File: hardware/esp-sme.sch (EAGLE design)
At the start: 37 parts, among them J2 BME280, J3 UART, Q1 MOSFET-NCH-AO3404A, Q2 MOSFET-NCH-AO3404A, Q3 NPN, Q4 NPN, Q5 NPN, U2 MIC5504

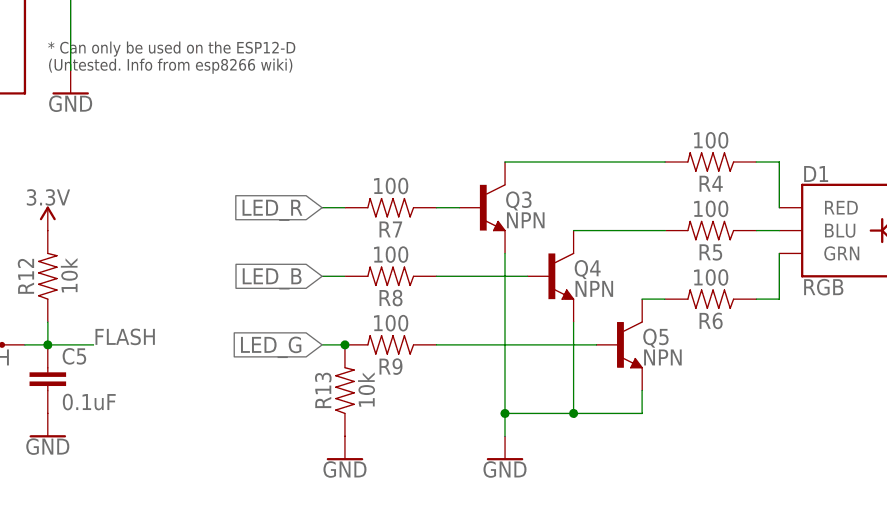
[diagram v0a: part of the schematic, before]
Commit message: Replaced transistor for n-channel mosfet
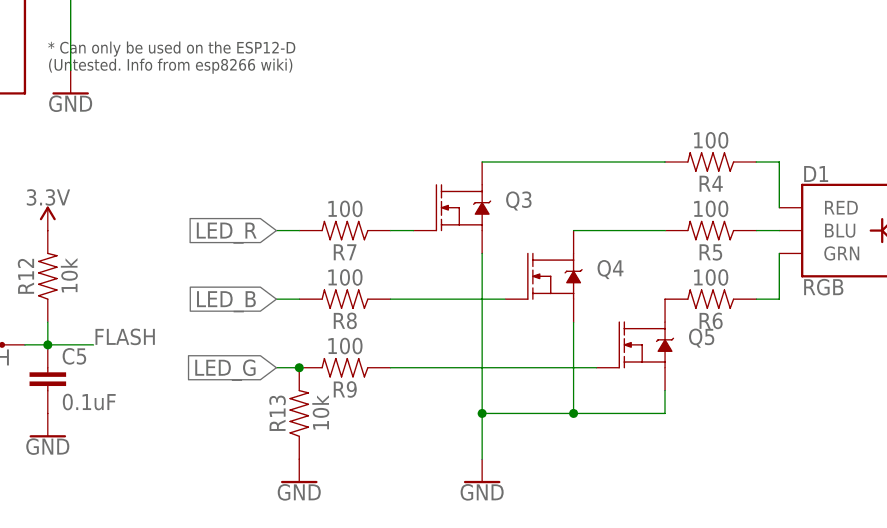
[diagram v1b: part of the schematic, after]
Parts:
- Q3, Q4, Q5: value NPN -> MOSFET-NCH-AO3404A; device SparkFun-DiscreteSemi:TRANS_NPN-MMBT2222AL -> SparkFun-DiscreteSemi:MOSFET-NCH-AO3404A
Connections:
- net GND: now also Q3.S, Q4.S, Q5.S; no longer Q3.E, Q4.E, Q5.E
- net N$4: now also Q5.D; no longer Q5.C
- net N$5: now also Q4.D; no longer Q4.C
- net N$6: now also Q3.D; no longer Q3.C
- net N$7: now also Q5.G; no longer Q5.B
- net N$8: now also Q4.G; no longer Q4.B
- net N$9: now also Q3.G; no longer Q3.B
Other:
- moved on the sheet: R13, R7, R8, R9
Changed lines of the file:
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@@
 <part name="R6" library="SparkFun-Resistors" library_urn="urn:adsk.eagle:library:532" deviceset="100OHM" device="-0603-1/10W-1%" package3d_urn="urn:adsk.eagle:package:39650/1" value="100"/>
 <part name="SUPPLY8" library="SparkFun-PowerSymbols" library_urn="urn:adsk.eagle:library:530" deviceset="3.3V" device=""/>
-<part name="Q3" library="SparkFun-DiscreteSemi" library_urn="urn:adsk.eagle:library:514" deviceset="TRANS_NPN" device="-MMBT2222AL" package3d_urn="urn:adsk.eagle:package:38446/1" value="NPN"/>
-<part name="Q4" library="SparkFun-DiscreteSemi" library_urn="urn:adsk.eagle:library:514" deviceset="TRANS_NPN" device="-MMBT2222AL" package3d_urn="urn:adsk.eagle:package:38446/1" value="NPN"/>
-<part name="Q5" library="SparkFun-DiscreteSemi" library_urn="urn:adsk.eagle:library:514" deviceset="TRANS_NPN" device="-MMBT2222AL" package3d_urn="urn:adsk.eagle:package:38446/1" value="NPN"/>
 <part name="R7" library="SparkFun-Resistors" library_urn="urn:adsk.eagle:library:532" deviceset="100OHM" device="-0603-1/10W-1%" package3d_urn="urn:adsk.eagle:package:39650/1" value="100"/>
 <part name="R8" library="SparkFun-Resistors" library_urn="urn:adsk.eagle:library:532" deviceset="100OHM" device="-0603-1/10W-1%" package3d_urn="urn:adsk.eagle:package:39650/1" value="100"/>
@@
 <part name="R14" library="SparkFun-Resistors" library_urn="urn:adsk.eagle:library:532" deviceset="10KOHM" device="-0603-1/10W-1%" package3d_urn="urn:adsk.eagle:package:39650/1" value="10k"/>
 <part name="R15" library="SparkFun-Resistors" library_urn="urn:adsk.eagle:library:532" deviceset="10KOHM" device="-0603-1/10W-1%" package3d_urn="urn:adsk.eagle:package:39650/1" value="10k"/>
+<part name="Q3" library="SparkFun-DiscreteSemi" library_urn="urn:adsk.eagle:library:514" deviceset="MOSFET-NCH" device="-AO3404A" package3d_urn="urn:adsk.eagle:package:38446/1" value=""/>
+<part name="Q4" library="SparkFun-DiscreteSemi" library_urn="urn:adsk.eagle:library:514" deviceset="MOSFET-NCH" device="-AO3404A" package3d_urn="urn:adsk.eagle:package:38446/1" value=""/>
+<part name="Q5" library="SparkFun-DiscreteSemi" library_urn="urn:adsk.eagle:library:514" deviceset="MOSFET-NCH" device="-AO3404A" package3d_urn="urn:adsk.eagle:package:38446/1" value=""/>
 </parts>
 <sheets>
@@
 <instance part="R6" gate="G$1" x="101.6" y="-10.16" rot="R180"/>
 <instance part="SUPPLY8" gate="G$1" x="132.08" y="5.08"/>
-<instance part="Q3" gate="G$1" x="76.2" y="0"/>
-<instance part="Q4" gate="G$1" x="83.82" y="-7.62"/>
-<instance part="Q5" gate="G$1" x="91.44" y="-15.24"/>
-<instance part="R7" gate="G$1" x="66.04" y="0" rot="R180"/>
-<instance part="R8" gate="G$1" x="66.04" y="-7.62" rot="R180"/>
-<instance part="R9" gate="G$1" x="66.04" y="-15.24" rot="R180"/>
-<instance part="GND9" gate="1" x="78.74" y="-27.94"/>
+<instance part="R7" gate="G$1" x="60.96" y="-2.54" rot="R180"/>
+<instance part="R8" gate="G$1" x="60.96" y="-10.16" rot="R180"/>
+<instance part="R9" gate="G$1" x="60.96" y="-17.78" rot="R180"/>
+<instance part="GND9" gate="1" x="76.2" y="-30.48"/>
 <instance part="J2" gate="G$1" x="86.36" y="38.1" rot="R180"/>
 <instance part="SUPPLY9" gate="G$1" x="78.74" y="50.8"/>
@@
 <instance part="C5" gate="G$1" x="27.94" y="-20.32"/>
 <instance part="GND15" gate="1" x="27.94" y="-25.4"/>
-<instance part="R13" gate="G$1" x="60.96" y="-20.32" rot="R90"/>
-<instance part="GND16" gate="1" x="60.96" y="-27.94"/>
+<instance part="R13" gate="G$1" x="55.88" y="-22.86" rot="R90"/>
+<instance part="GND16" gate="1" x="55.88" y="-30.48"/>
 <instance part="R14" gate="G$1" x="73.66" y="45.72" rot="R90"/>
 <instance part="R15" gate="G$1" x="66.04" y="45.72" rot="R90"/>
+<instance part="Q3" gate="NMOS" x="73.66" y="0"/>
+<instance part="Q4" gate="NMOS" x="83.82" y="-7.62"/>
+<instance part="Q5" gate="NMOS" x="93.98" y="-15.24"/>
 </instances>
 <busses>
@@
 </segment>
 <segment>
-<pinref part="Q3" gate="G$1" pin="E"/>
-<wire x1="78.74" y1="-5.08" x2="78.74" y2="-22.86" width="0.1524" layer="91"/>
+<wire x1="76.2" y1="-5.08" x2="76.2" y2="-22.86" width="0.1524" layer="91"/>
 <pinref part="GND9" gate="1" pin="GND"/>
-<pinref part="Q4" gate="G$1" pin="E"/>
-<wire x1="78.74" y1="-22.86" x2="78.74" y2="-25.4" width="0.1524" layer="91"/>
+<wire x1="76.2" y1="-22.86" x2="76.2" y2="-27.94" width="0.1524" layer="91"/>
 <wire x1="86.36" y1="-12.7" x2="86.36" y2="-22.86" width="0.1524" layer="91"/>
-<pinref part="Q5" gate="G$1" pin="E"/>
-<wire x1="93.98" y1="-20.32" x2="93.98" y2="-22.86" width="0.1524" layer="91"/>
-<wire x1="93.98" y1="-22.86" x2="86.36" y2="-22.86" width="0.1524" layer="91"/>
-<wire x1="86.36" y1="-22.86" x2="78.74" y2="-22.86" width="0.1524" layer="91"/>
+<wire x1="96.52" y1="-20.32" x2="96.52" y2="-22.86" width="0.1524" layer="91"/>
+<wire x1="96.52" y1="-22.86" x2="86.36" y2="-22.86" width="0.1524" layer="91"/>
+<wire x1="86.36" y1="-22.86" x2="76.2" y2="-22.86" width="0.1524" layer="91"/>
 <junction x="86.36" y="-22.86"/>
-<junction x="78.74" y="-22.86"/>
+<junction x="76.2" y="-22.86"/>
+<pinref part="Q3" gate="NMOS" pin="S"/>
+<pinref part="Q4" gate="NMOS" pin="S"/>
+<pinref part="Q5" gate="NMOS" pin="S"/>
 </segment>
 <segment>
@@
 <segment>
 <pinref part="R7" gate="G$1" pin="2"/>
-<wire x1="60.96" y1="0" x2="58.42" y2="0" width="0.1524" layer="91"/>
-<label x="58.42" y="0" size="1.778" layer="95" rot="R180" xref="yes"/>
+<wire x1="55.88" y1="-2.54" x2="53.34" y2="-2.54" width="0.1524" layer="91"/>
+<label x="53.34" y="-2.54" size="1.778" layer="95" rot="R180" xref="yes"/>
 </segment>
 </net>
@@
 <segment>
 <pinref part="R8" gate="G$1" pin="2"/>
-<wire x1="60.96" y1="-7.62" x2="58.42" y2="-7.62" width="0.1524" layer="91"/>
-<label x="58.42" y="-7.62" size="1.778" layer="95" rot="R180" xref="yes"/>
+<wire x1="55.88" y1="-10.16" x2="53.34" y2="-10.16" width="0.1524" layer="91"/>
+<label x="53.34" y="-10.16" size="1.778" layer="95" rot="R180" xref="yes"/>
 </segment>
 </net>
@@
 <segment>
 <pinref part="R9" gate="G$1" pin="2"/>
-<wire x1="60.96" y1="-15.24" x2="58.42" y2="-15.24" width="0.1524" layer="91"/>
-<label x="58.42" y="-15.24" size="1.778" layer="95" rot="R180" xref="yes"/>
+<wire x1="55.88" y1="-17.78" x2="53.34" y2="-17.78" width="0.1524" layer="91"/>
+<label x="53.34" y="-17.78" size="1.778" layer="95" rot="R180" xref="yes"/>
 <pinref part="R13" gate="G$1" pin="2"/>
-<junction x="60.96" y="-15.24"/>
-</segment>
-</net>
-<net name="N$4" class="0">
-<segment>
-<pinref part="R6" gate="G$1" pin="2"/>
-<pinref part="Q5" gate="G$1" pin="C"/>
-<wire x1="96.52" y1="-10.16" x2="93.98" y2="-10.16" width="0.1524" layer="91"/>
+<junction x="55.88" y="-17.78"/>
 </segment>
 </net>
@@
 <segment>
 <pinref part="R5" gate="G$1" pin="2"/>
-<pinref part="Q4" gate="G$1" pin="C"/>
 <wire x1="96.52" y1="-2.54" x2="86.36" y2="-2.54" width="0.1524" layer="91"/>
+<pinref part="Q4" gate="NMOS" pin="D"/>
 </segment>
 </net>
 <net name="N$6" class="0">
 <segment>
-<pinref part="Q3" gate="G$1" pin="C"/>
 <pinref part="R4" gate="G$1" pin="2"/>
-<wire x1="96.52" y1="5.08" x2="78.74" y2="5.08" width="0.1524" layer="91"/>
+<wire x1="96.52" y1="5.08" x2="76.2" y2="5.08" width="0.1524" layer="91"/>
+<pinref part="Q3" gate="NMOS" pin="D"/>
 </segment>
 </net>
@@
 <net name="N$7" class="0">
 <segment>
-<pinref part="Q5" gate="G$1" pin="B"/>
-<wire x1="88.9" y1="-15.24" x2="71.12" y2="-15.24" width="0.1524" layer="91"/>
+<wire x1="88.9" y1="-17.78" x2="66.04" y2="-17.78" width="0.1524" layer="91"/>
 <pinref part="R9" gate="G$1" pin="1"/>
+<pinref part="Q5" gate="NMOS" pin="G"/>
 </segment>
 </net>
 <net name="N$8" class="0">
 <segment>
-<pinref part="Q4" gate="G$1" pin="B"/>
-<wire x1="81.28" y1="-7.62" x2="71.12" y2="-7.62" width="0.1524" layer="91"/>
+<wire x1="78.74" y1="-10.16" x2="66.04" y2="-10.16" width="0.1524" layer="91"/>
 <pinref part="R8" gate="G$1" pin="1"/>
+<pinref part="Q4" gate="NMOS" pin="G"/>
 </segment>
 </net>
 <net name="N$9" class="0">
 <segment>
-<pinref part="Q3" gate="G$1" pin="B"/>
-<wire x1="73.66" y1="0" x2="71.12" y2="0" width="0.1524" layer="91"/>
+<wire x1="68.58" y1="-2.54" x2="66.04" y2="-2.54" width="0.1524" layer="91"/>
 <pinref part="R7" gate="G$1" pin="1"/>
+<pinref part="Q3" gate="NMOS" pin="G"/>
 </segment>
 </net>
@@
 </segment>
 </net>
+<net name="N$4" class="0">
+<segment>
+<pinref part="R6" gate="G$1" pin="2"/>
+<pinref part="Q5" gate="NMOS" pin="D"/>
+</segment>
+</net>
